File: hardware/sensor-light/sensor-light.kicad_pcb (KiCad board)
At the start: 2 copper layers, 15 parts, among them J1 Power IN 12V, J2 PIR Sensor 2, J3 PIR Sensor 1, J4 PROG Header, J5 Light Sensor, J6 PWM Power OUT 12V, Q1 IRLML2502, SW1 Manual ON/OFF, U1 Reg 3.3V, U2 MSP430G2553IN20

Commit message: attempt to place components on the PCB
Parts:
- added R3: 56 Ohm, Resistors_THT:R_Axial_DIN0411_L9.9mm_D3.6mm_P12.70mm_Horizontal, F.Cu at (172.7, 111.8)
- added R4: 56 Ohm, Resistors_THT:R_Axial_DIN0411_L9.9mm_D3.6mm_P12.70mm_Horizontal, F.Cu at (172.7, 133.3)
- C1: footprint Capacitors_THT:CP_Radial_D4.0mm_P2.00mm -> Capacitors_THT:CP_Radial_D5.0mm_P2.50mm
- D1, D2: footprint LEDs:LED_CREE-XQ_HandSoldering -> LEDs:LED_D3.0mm
- J1, J6: footprint Socket_Strips:Socket_Strip_Straight_1x02_Pitch2.54mm -> Connectors:AK300-2
- R1, R2: footprint Resistors_SMD:R_1218_HandSoldering -> Resistors_THT:R_Axial_DIN0411_L9.9mm_D3.6mm_P12.70mm_Horizontal
- SW1: footprint Buttons_Switches_THT:SW_PUSH_SMALL -> Buttons_Switches_THT:SW_PUSH_6mm_h5mm
- moved J6 91.5 mm to (108.0, 119.4), turned to 90 degrees
- moved Q1 89.7 mm to (124.5, 112.4), turned to 90 degrees
- moved R2 79.4 mm to (124.5, 121.3), turned to 270 degrees
- moved J5 75.0 mm to (178.4, 125.1), turned to 180 degrees
- moved R1 66.2 mm to (131.4, 111.8)
- moved J1 59.1 mm to (108.0, 134.0), turned to 90 degrees
- moved C1 58.5 mm to (144.8, 131.4), turned to 270 degrees
- moved U1 58.4 mm to (134.0, 131.4), turned to 180 degrees
- moved J4 51.8 mm to (146.7, 125.1), turned to 180 degrees
- moved SW1 41.2 mm to (187.3, 120.7)
- moved J3 41.0 mm to (152.4, 111.1)
- moved U2 36.8 mm to (166.4, 134.0), turned to 180 degrees
- moved D1 19.3 mm to (194.3, 111.8), turned to 180 degrees
- moved D2 17.2 mm to (194.3, 133.3), turned to 180 degrees
- moved J2 13.5 mm to (152.4, 134.0), turned to 180 degrees
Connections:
- J1 pad 1: Net-(J1-Pad1) -> Net-(C1-Pad2)
- J1 pad 2: Net-(C1-Pad2) -> Net-(J1-Pad2)
- J2 pad 1: Net-(C1-Pad1) -> Net-(C1-Pad2)
- J2 pad 3: Net-(C1-Pad2) -> Net-(C1-Pad1)
- J3 pad 1: Net-(C1-Pad1) -> Net-(C1-Pad2)
- J3 pad 3: Net-(C1-Pad2) -> Net-(C1-Pad1)
- J4 pad 1: Net-(C1-Pad1) -> Net-(C1-Pad2)
- J4 pad 4: Net-(C1-Pad2) -> Net-(C1-Pad1)
- J5 pad 2: Net-(J5-Pad2) -> Net-(C1-Pad1)
- J5 pad 3: Net-(C1-Pad1) -> Net-(J5-Pad3)
- J6 pad 1: Net-(J1-Pad1) -> Net-(J1-Pad2)
- U1 pad 3: Net-(J1-Pad1) -> Net-(J1-Pad2)
- U2 pad 10: Net-(U2-Pad10) -> (no net)
- U2 pad 11: Net-(U2-Pad11) -> (no net)
- U2 pad 14: Net-(D1-Pad2) -> Net-(R3-Pad1)
- U2 pad 15: Net-(U2-Pad15) -> (no net)
- U2 pad 18: Net-(U2-Pad18) -> (no net)
- U2 pad 19: Net-(U2-Pad19) -> (no net)
- U2 pad 2: Net-(D2-Pad2) -> Net-(R4-Pad1)
- U2 pad 3: Net-(U2-Pad3) -> (no net)
- U2 pad 6: Net-(J5-Pad2) -> Net-(J5-Pad3)
- U2 pad 7: Net-(U2-Pad7) -> (no net)
- U2 pad 8: Net-(U2-Pad8) -> (no net)
- U2 pad 9: Net-(U2-Pad9) -> (no net)

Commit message: some attempt of pcb routing
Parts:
- removed R1: 27 Ohm, Resistors_THT:R_Axial_DIN0411_L9.9mm_D3.6mm_P12.70mm_Horizontal
- removed R2: 100 KOhm, Resistors_THT:R_Axial_DIN0411_L9.9mm_D3.6mm_P12.70mm_Horizontal
- J2: value PIR Sensor 2 -> PIR 2
- J3: value PIR Sensor 1 -> PIR 1
- J6: value PWM Power OUT 12V -> Power OUT 12V
- moved J2 17.8 mm to (153.7, 116.2)
- moved J1 16.6 mm to (124.5, 132.7)
- moved J6 16.6 mm to (124.5, 118.1)
- moved Q1 10.8 mm to (135.3, 112.4)
- moved J3 9.69 mm to (144.1, 116.2), turned to 180 degrees
- moved J4 9.44 mm to (153.7, 131.4)
- moved J5 6.99 mm to (171.4, 125.1)
- moved U1 3.86 mm to (137.8, 132.1)
- moved SW1 3.24 mm to (184.2, 120.0)
- moved D1 3.18 mm to (191.1, 111.8)
- moved D2 3.18 mm to (191.1, 133.3)
- moved C1 2.54 mm to (147.3, 131.4)
- moved R3 1.27 mm to (171.4, 111.8)
- moved R4 1.27 mm to (171.4, 133.3)
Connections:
- J6 pad 1: Net-(J1-Pad2) -> Net-(J6-Pad1)
- J6 pad 2: Net-(J6-Pad2) -> Net-(J1-Pad2)
- Q1 pad 1: Net-(J6-Pad2) -> Net-(J6-Pad1)
- U2 pad 4: Net-(R1-Pad2) -> Net-(Q1-Pad2)
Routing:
- net Net-(C1-Pad2): track 0.00 -> 182.9 mm, vias 0 -> 3
- net Net-(C1-Pad1): track 0.00 -> 107.5 mm, vias 0 -> 3
- net Net-(Q1-Pad2): track 0.00 -> 49.2 mm, vias 0 -> 1
- net Net-(J1-Pad2): track 0.00 -> 35.5 mm, vias 0 -> 1
- net Net-(SW1-Pad1): track 0.00 -> 29.2 mm, vias 0 -> 1
- net Net-(R3-Pad1): track 0.00 -> 20.7 mm, vias 0 -> 1
- net Net-(J3-Pad2): track 0.00 -> 19.8 mm, vias 0 -> 1
- net Net-(J6-Pad1): track 0.00 -> 13.1 mm, vias 0 -> 1
- net Net-(J4-Pad2): track 0.00 -> 6.13 mm
- net Net-(J4-Pad3): track 0.00 -> 6.13 mm
- net Net-(J2-Pad2): track 0.00 -> 6.13 mm
- net Net-(R4-Pad1): track 0.00 -> 5.87 mm
- net Net-(J5-Pad3): track 0.00 -> 5.61 mm
- net Net-(D2-Pad2): track 0.00 -> 4.44 mm
- net Net-(D1-Pad2): track 0.00 -> 4.44 mm
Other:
- board outline added: 78.1 x 31.1 mm
- net class Default: clearance 0.2 -> 0.5; trace_width 0.25 -> 0.5
- rule trace_clearance: 0.2 -> 0.5

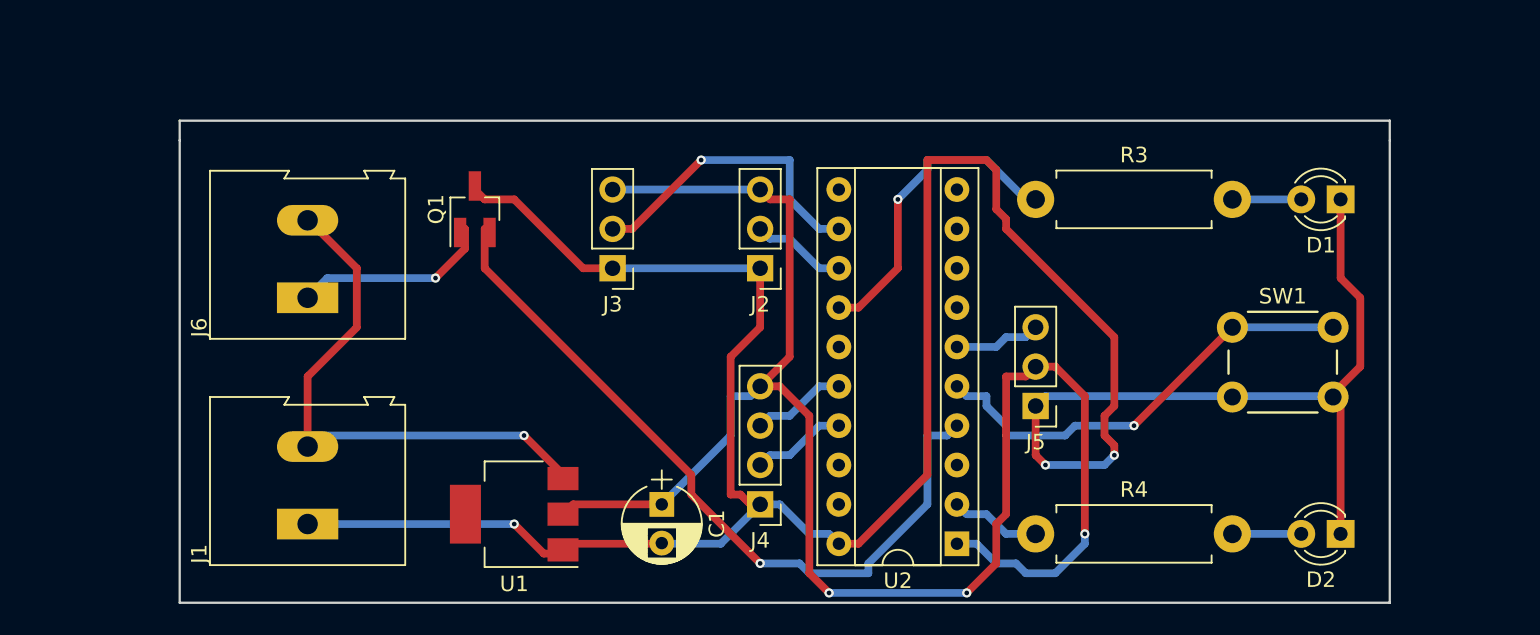
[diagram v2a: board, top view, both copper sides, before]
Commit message: Attempt at laying out the board
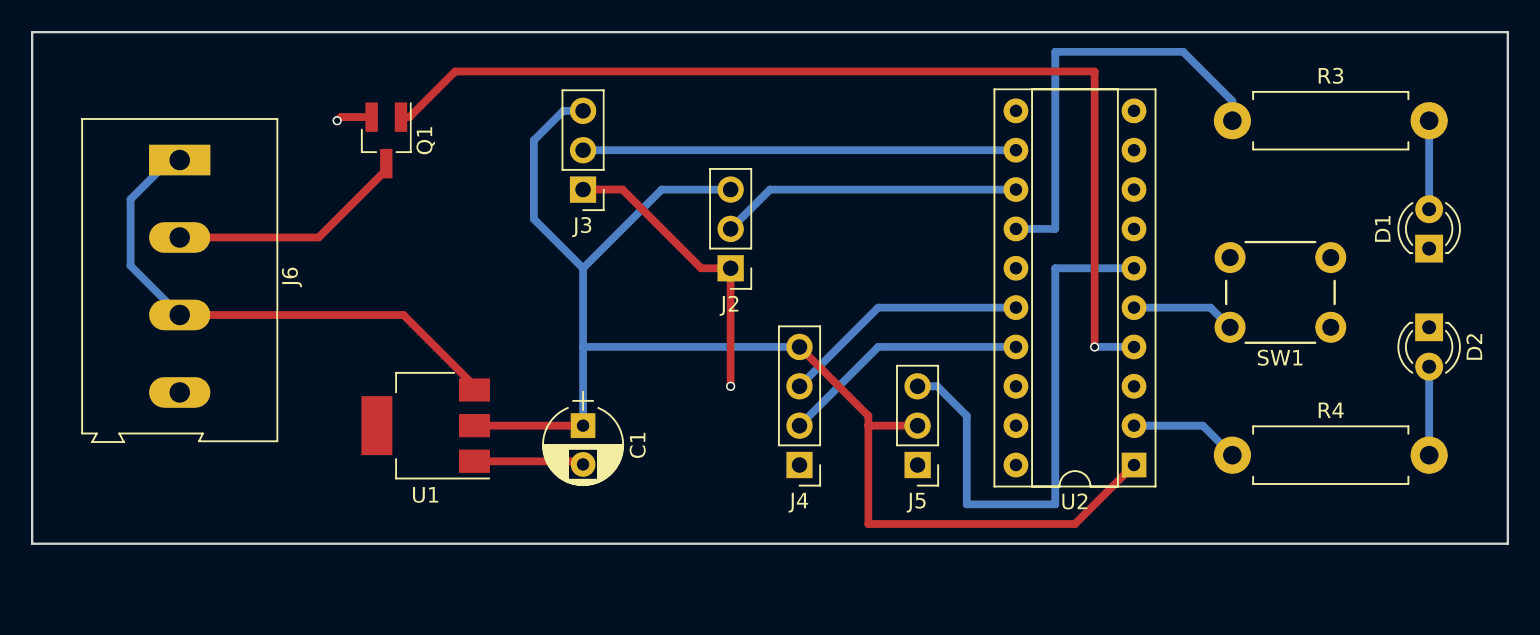
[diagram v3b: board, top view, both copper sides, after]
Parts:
- removed J1: Power IN 12V, Connectors:AK300-2
- J2: value PIR 2 -> PIR Sensor 2
- J3: value PIR 1 -> PIR Sensor 1
- J6: value Power OUT 12V -> Power IN/OUT 12V; footprint Connectors:AK300-2 -> Connectors:AK300-4
- R3: value 56 Ohm -> 47Ω
- R4: value 56 Ohm -> 27Ω
- moved D2 14.5 mm to (196.8, 120.0), turned to 270 degrees
- moved R3 13.7 mm to (184.2, 106.7)
- moved R4 13.7 mm to (184.2, 128.3)
- moved U2 12.5 mm to (177.8, 128.9)
- moved J6 12.1 mm to (116.2, 109.2), turned to 270 degrees
- moved J5 8.52 mm to (163.8, 128.9)
- moved U1 8.08 mm to (132.1, 126.4)
- moved Q1 7.24 mm to (129.5, 108.0), turned to 270 degrees
- moved C1 7.18 mm to (142.2, 126.4)
- moved D1 6.54 mm to (196.8, 114.9), turned to 90 degrees
- moved SW1 6.35 mm to (190.5, 120.0), turned to 180 degrees
- moved J3 5.43 mm to (142.2, 111.1)
- moved J4 3.59 mm to (156.2, 128.9)
- moved J2 1.91 mm to (151.8, 116.2)
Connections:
- J6 pad 2: Net-(J1-Pad2) -> Net-(J6-Pad2)
- Q1 pad 1: Net-(J6-Pad1) -> Net-(Q1-Pad1)
- Q1 pad 2: Net-(Q1-Pad2) -> Net-(C1-Pad2)
- Q1 pad 3: Net-(C1-Pad2) -> Net-(J6-Pad2)
- U1 pad 3: Net-(J1-Pad2) -> Net-(J6-Pad1)
- U2 pad 4: Net-(Q1-Pad2) -> Net-(Q1-Pad1)
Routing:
- net Net-(C1-Pad2): track 182.9 -> 28.7 mm, vias 3 -> 2
- net Net-(Q1-Pad1): track 0.00 -> 66.3 mm, vias 0 -> 1
- net Net-(Q1-Pad2): track 49.2 -> 0.00 mm, vias 1 -> 0
- net Net-(J1-Pad2): track 35.5 -> 0.00 mm, vias 1 -> 0
- net Net-(J5-Pad3): track 5.61 -> 36.3 mm
- net Net-(SW1-Pad1): track 29.2 -> 6.73 mm, vias 1 -> 0
- net Net-(J6-Pad1): track 13.1 -> 34.2 mm, vias 1 -> 0
- net Net-(C1-Pad1): track 107.5 -> 91.5 mm, vias 3 -> 0
- net Net-(J6-Pad2): track 0.00 -> 15.5 mm
- net Net-(J2-Pad2): track 6.13 -> 19.5 mm
- net Net-(J4-Pad3): track 6.13 -> 16.1 mm
- net Net-(J4-Pad2): track 6.13 -> 16.1 mm
- net Net-(J3-Pad2): track 19.8 -> 27.9 mm, vias 1 -> 0
- net Net-(R3-Pad1): track 20.7 -> 28.0 mm, vias 1 -> 0
- net Net-(R4-Pad1): track 5.87 -> 7.14 mm
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- added copper zone on B.Cu, net Net-(C1-Pad2)
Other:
- board size 78.1 x 31.1 mm -> 95.2 x 33 mm

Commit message: try adust layout
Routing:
- net Net-(C1-Pad1): track 91.5 -> 21.3 mm
- net Net-(C1-Pad2): track 28.7 -> 9.41 mm, vias 2 -> 1
- net Net-(Q1-Pad1): track 66.3 -> 68.3 mm, vias 1 -> 0
- added copper zone on F.Cu, net Net-(C1-Pad1)
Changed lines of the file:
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@@
     (thickness 1.6)
     (drawings 4)
-    (tracks 67)
+    (tracks 48)
     (zones 0)
     (modules 14)
@@
   (gr_line (start 201.93 100.965) (end 106.68 100.965) (angle 90) (layer Edge.Cuts) (width 0.15))
   (gr_line (start 201.93 133.985) (end 201.93 100.965) (angle 90) (layer Edge.Cuts) (width 0.15))
-  (segment (start 160.655 126.365) (end 160.655 125.73) (width 0.5) (layer F.Cu) (net 1))
-  (segment (start 160.655 125.73) (end 156.21 121.285) (width 0.5) (layer F.Cu) (net 1) (status 800000))
-  (segment (start 177.8 128.905) (end 173.99 132.715) (width 0.5) (layer F.Cu) (net 1) (status 400000))
-  (segment (start 160.655 126.365) (end 163.83 126.365) (width 0.5) (layer F.Cu) (net 1) (status 800000))
-  (segment (start 160.655 132.715) (end 160.655 126.365) (width 0.5) (layer F.Cu) (net 1))
-  (segment (start 173.99 132.715) (end 160.655 132.715) (width 0.5) (layer F.Cu) (net 1))
-  (segment (start 151.765 111.125) (end 147.32 111.125) (width 0.5) (layer B.Cu) (net 1))
-  (segment (start 147.32 111.125) (end 142.24 116.205) (width 0.5) (layer B.Cu) (net 1))
-  (segment (start 156.21 121.285) (end 142.24 121.285) (width 0.5) (layer B.Cu) (net 1))
-  (segment (start 142.24 126.365) (end 142.24 121.285) (width 0.5) (layer B.Cu) (net 1))
-  (segment (start 142.24 121.285) (end 142.24 116.205) (width 0.5) (layer B.Cu) (net 1))
-  (segment (start 140.97 106.045) (end 142.24 106.045) (width 0.5) (layer B.Cu) (net 1))
-  (segment (start 139.065 107.95) (end 140.97 106.045) (width 0.5) (layer B.Cu) (net 1))
-  (segment (start 139.065 113.03) (end 139.065 107.95) (width 0.5) (layer B.Cu) (net 1))
-  (segment (start 142.24 116.205) (end 139.065 113.03) (width 0.5) (layer B.Cu) (net 1))
+  (segment (start 165.1 132.715) (end 173.99 132.715) (width 0.5) (layer F.Cu) (net 1))
+  (segment (start 173.99 132.715) (end 177.8 128.905) (width 0.5) (layer F.Cu) (net 1))
   (segment (start 135.23 126.365) (end 142.24 126.365) (width 0.5) (layer F.Cu) (net 1))
-  (segment (start 151.765 116.205) (end 151.765 123.825) (width 0.5) (layer F.Cu) (net 2) (status 400000))
-  (via (at 151.765 123.825) (size 0.6) (drill 0.4) (layers F.Cu B.Cu) (net 2))
-  (segment (start 142.24 111.125) (end 144.78 111.125) (width 0.5) (layer F.Cu) (net 2) (status 400000))
-  (segment (start 149.86 116.205) (end 151.765 116.205) (width 0.5) (layer F.Cu) (net 2) (status 800000))
-  (segment (start 144.78 111.125) (end 149.86 116.205) (width 0.5) (layer F.Cu) (net 2))
-  (segment (start 128.59 106.45) (end 126.595 106.45) (width 0.5) (layer F.Cu) (net 2) (status 400000))
+  (segment (start 128.59 106.45) (end 126.595 106.45) (width 0.5) (layer F.Cu) (net 2))
   (via (at 126.365 106.68) (size 0.6) (drill 0.4) (layers F.Cu B.Cu) (net 2))
   (segment (start 126.595 106.45) (end 126.365 106.68) (width 0.5) (layer F.Cu) (net 2))
-  (segment (start 135.23 128.665) (end 142.04 128.665) (width 0.5) (layer F.Cu) (net 2) (status C00000))
-  (segment (start 142.04 128.665) (end 142.24 128.865) (width 0.5) (layer F.Cu) (net 2) (status C00000))
+  (segment (start 135.23 128.665) (end 142.04 128.665) (width 0.5) (layer F.Cu) (net 2))
+  (segment (start 142.04 128.665) (end 142.24 128.865) (width 0.5) (layer F.Cu) (net 2))
   (segment (start 196.85 112.395) (end 196.85 106.68) (width 0.5) (layer B.Cu) (net 3))
   (segment (start 196.85 128.27) (end 196.85 122.555) (width 0.5) (layer B.Cu) (net 4))
@@
   (segment (start 129.54 109.855) (end 125.175 114.22) (width 0.5) (layer F.Cu) (net 14))
   (segment (start 125.175 114.22) (end 116.205 114.22) (width 0.5) (layer F.Cu) (net 14))
-  (segment (start 175.26 103.505) (end 175.26 121.285) (width 0.5) (layer F.Cu) (net 15))
-  (segment (start 131.04 106.45) (end 133.985 103.505) (width 0.5) (layer F.Cu) (net 15))
-  (segment (start 133.985 103.505) (end 175.26 103.505) (width 0.5) (layer F.Cu) (net 15))
-  (segment (start 130.49 106.45) (end 131.04 106.45) (width 0.5) (layer F.Cu) (net 15))
-  (segment (start 175.26 121.285) (end 177.8 121.285) (width 0.5) (layer B.Cu) (net 15))
-  (via (at 175.26 121.285) (size 0.6) (drill 0.4) (layers F.Cu B.Cu) (net 15))
+  (segment (start 175.26 102.235) (end 135.255 102.235) (width 0.5) (layer F.Cu) (net 15))
+  (segment (start 177.8 121.285) (end 175.26 121.285) (width 0.5) (layer F.Cu) (net 15))
+  (segment (start 175.26 102.235) (end 175.26 121.285) (width 0.5) (layer F.Cu) (net 15))
+  (segment (start 135.255 102.235) (end 130.81 106.68) (width 0.5) (layer F.Cu) (net 15))
+  (segment (start 130.81 106.68) (end 130.49 106.45) (width 0.5) (layer F.Cu) (net 15))
   (zone (net 2) (net_name "Net-(C1-Pad2)") (layer B.Cu) (hatch edge 0.508)
     (connect_pads (clearance 0.508))
@@
       )
     )
+  )
+  (zone (net 1) (net_name "Net-(C1-Pad1)") (layer F.Cu) (hatch edge 0.508)
+    (connect_pads (clearance 0.508))
+    (min_thickness 0.254)
+    (fill yes (arc_segments 16) (thermal_gap 0.508) (thermal_bridge_width 0.508))
+    (polygon
+      (pts
+        (xy 137.795 133.985) (xy 137.795 104.14) (xy 166.37 104.14) (xy 166.37 133.985)
+      )
+    )
